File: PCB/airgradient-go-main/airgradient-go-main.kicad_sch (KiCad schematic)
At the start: 198 parts, among them CN3 SM05B-SRSS-TB (LF)(SN), CN4 SM05B-SRSS-TB (LF)(SN), CN5 SM05B-SRSS-TB (LF)(SN), Q1 SIA445EDJ-T1-GE3, Q2 ZVN4106FTA_C508255, Q3 CSD83325L, Q4 SS8050-G, Q5 SI1308EDL, SW1 TS-1091C-A1B3-D2, SW2 TS-1091C-A1B3-D2, U1 W25N512GVEIG, U10 SGP41-D-R4, U11 PS1-CO-SMOKE-10k, U12 SHT4x, U13 SPL07-003, U14 LIS2DH12TR, U15 TMUX121NKGR_C22428404, U16 S12, U17 TCA6408ARGT, U18 TAU1113, U19 LM66200DRLR, U2 ZDSD512MLGEAG, U20 LP5036, U3 BQ27742YZFR-G1, U4 ESP32-C5-MINI-1, U5 BQ25628RYKR, U6 HYG-8503A, U7 TPL5010DDCR, U8 TPS63802DLAR, U9 TPS7A0228DQNR

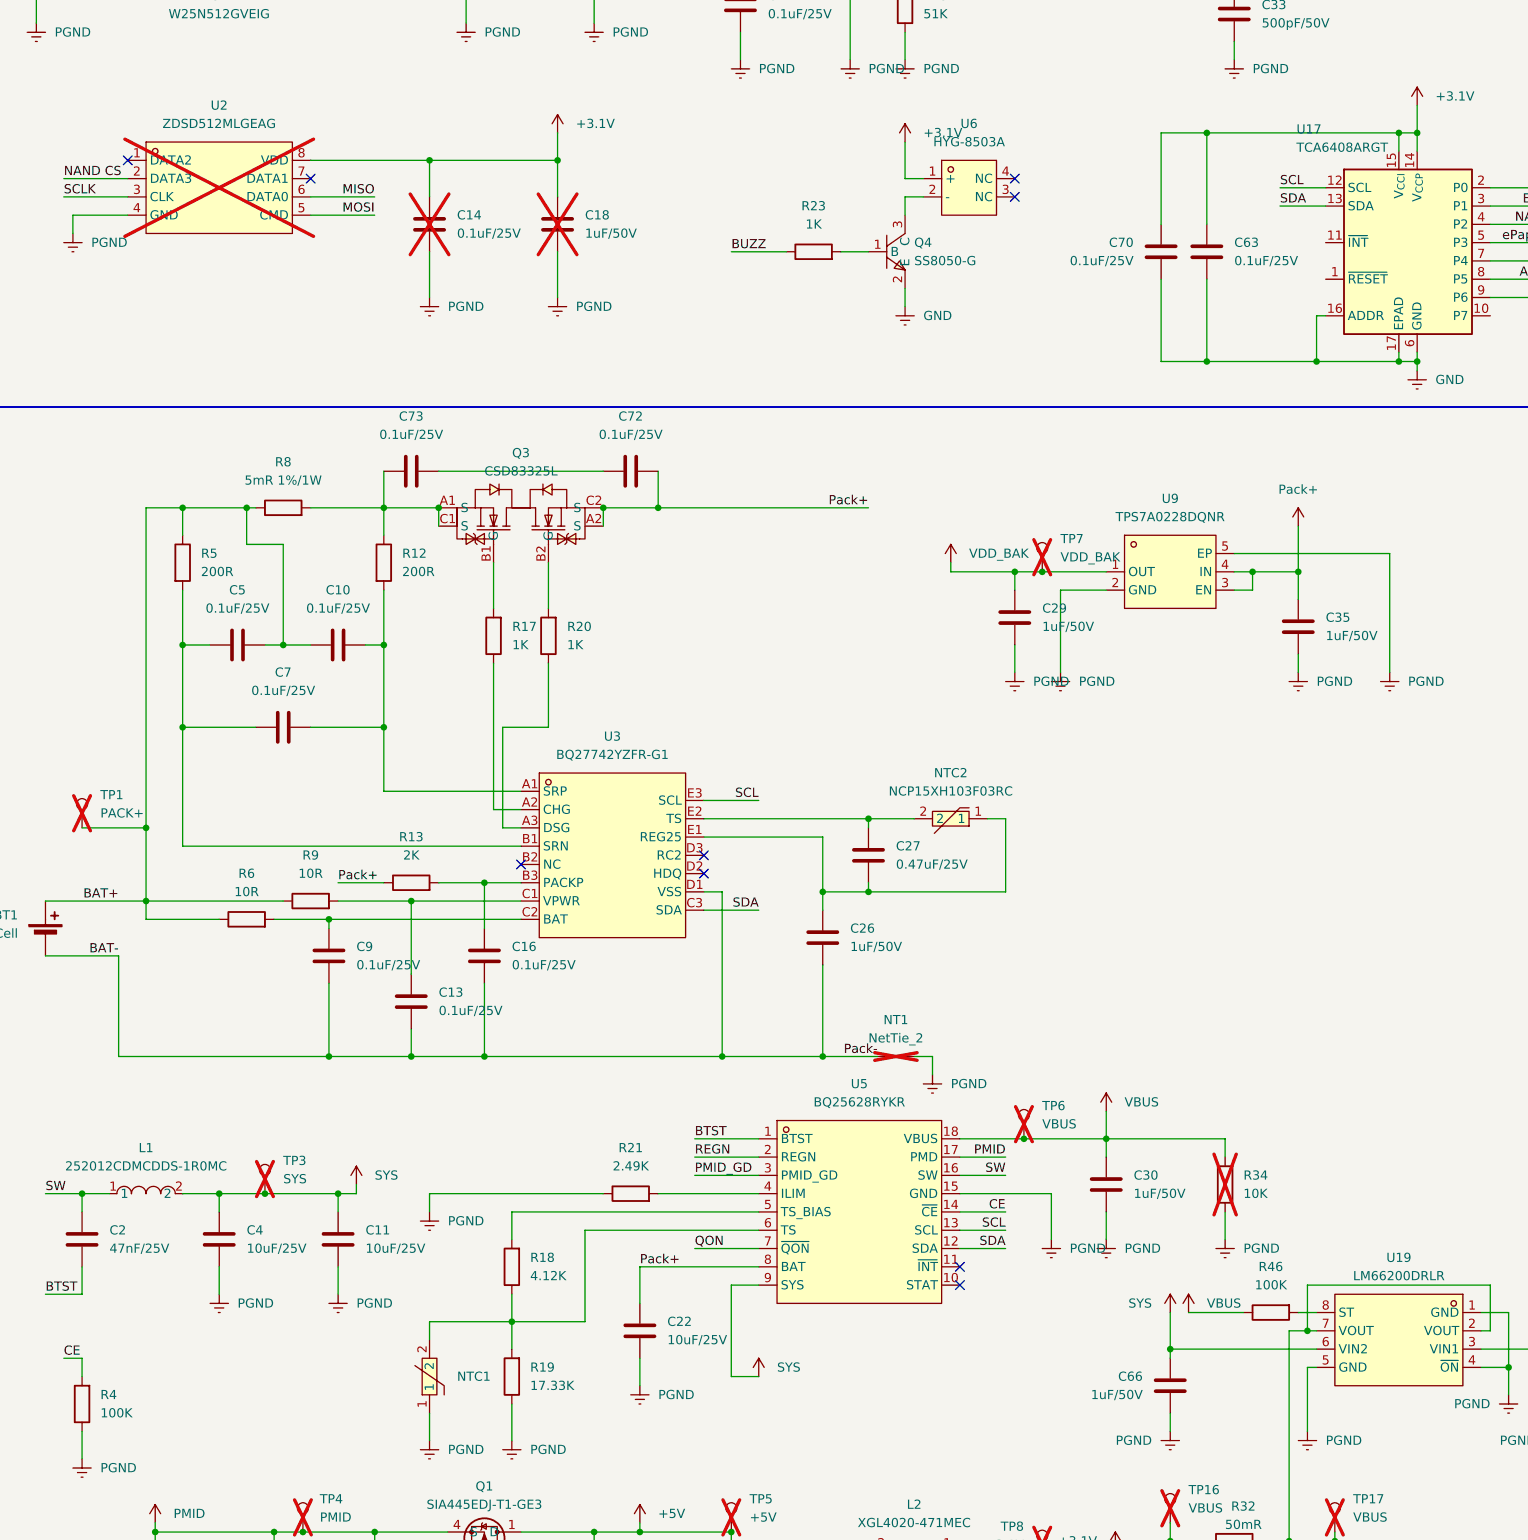
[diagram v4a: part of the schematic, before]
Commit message: v2.1: post-prototype fixes from v2.0 review and issue #1
- Battery: add C75 (100nF 0402) from BAT+ to GND at the battery +
  terminal as an RF shunt, with a GND via next to it
- NTC1 moved next to the battery negative tab (B.Cu), part changed
  to NCP15XH103F03RC; BQ25628 TS divider R18/R19 = 5.23k/30.1k
- Add R60 100K pull-up on TCA6408 RESET
- BOM: fix LCSC part numbers that were shared across different values
  (R13 2K -> C4109, R5/R12 200R -> C25087, 100K group -> C60491,
  C17/C21/C27 corrected)
- Remove test point footprints that were placed outside the board
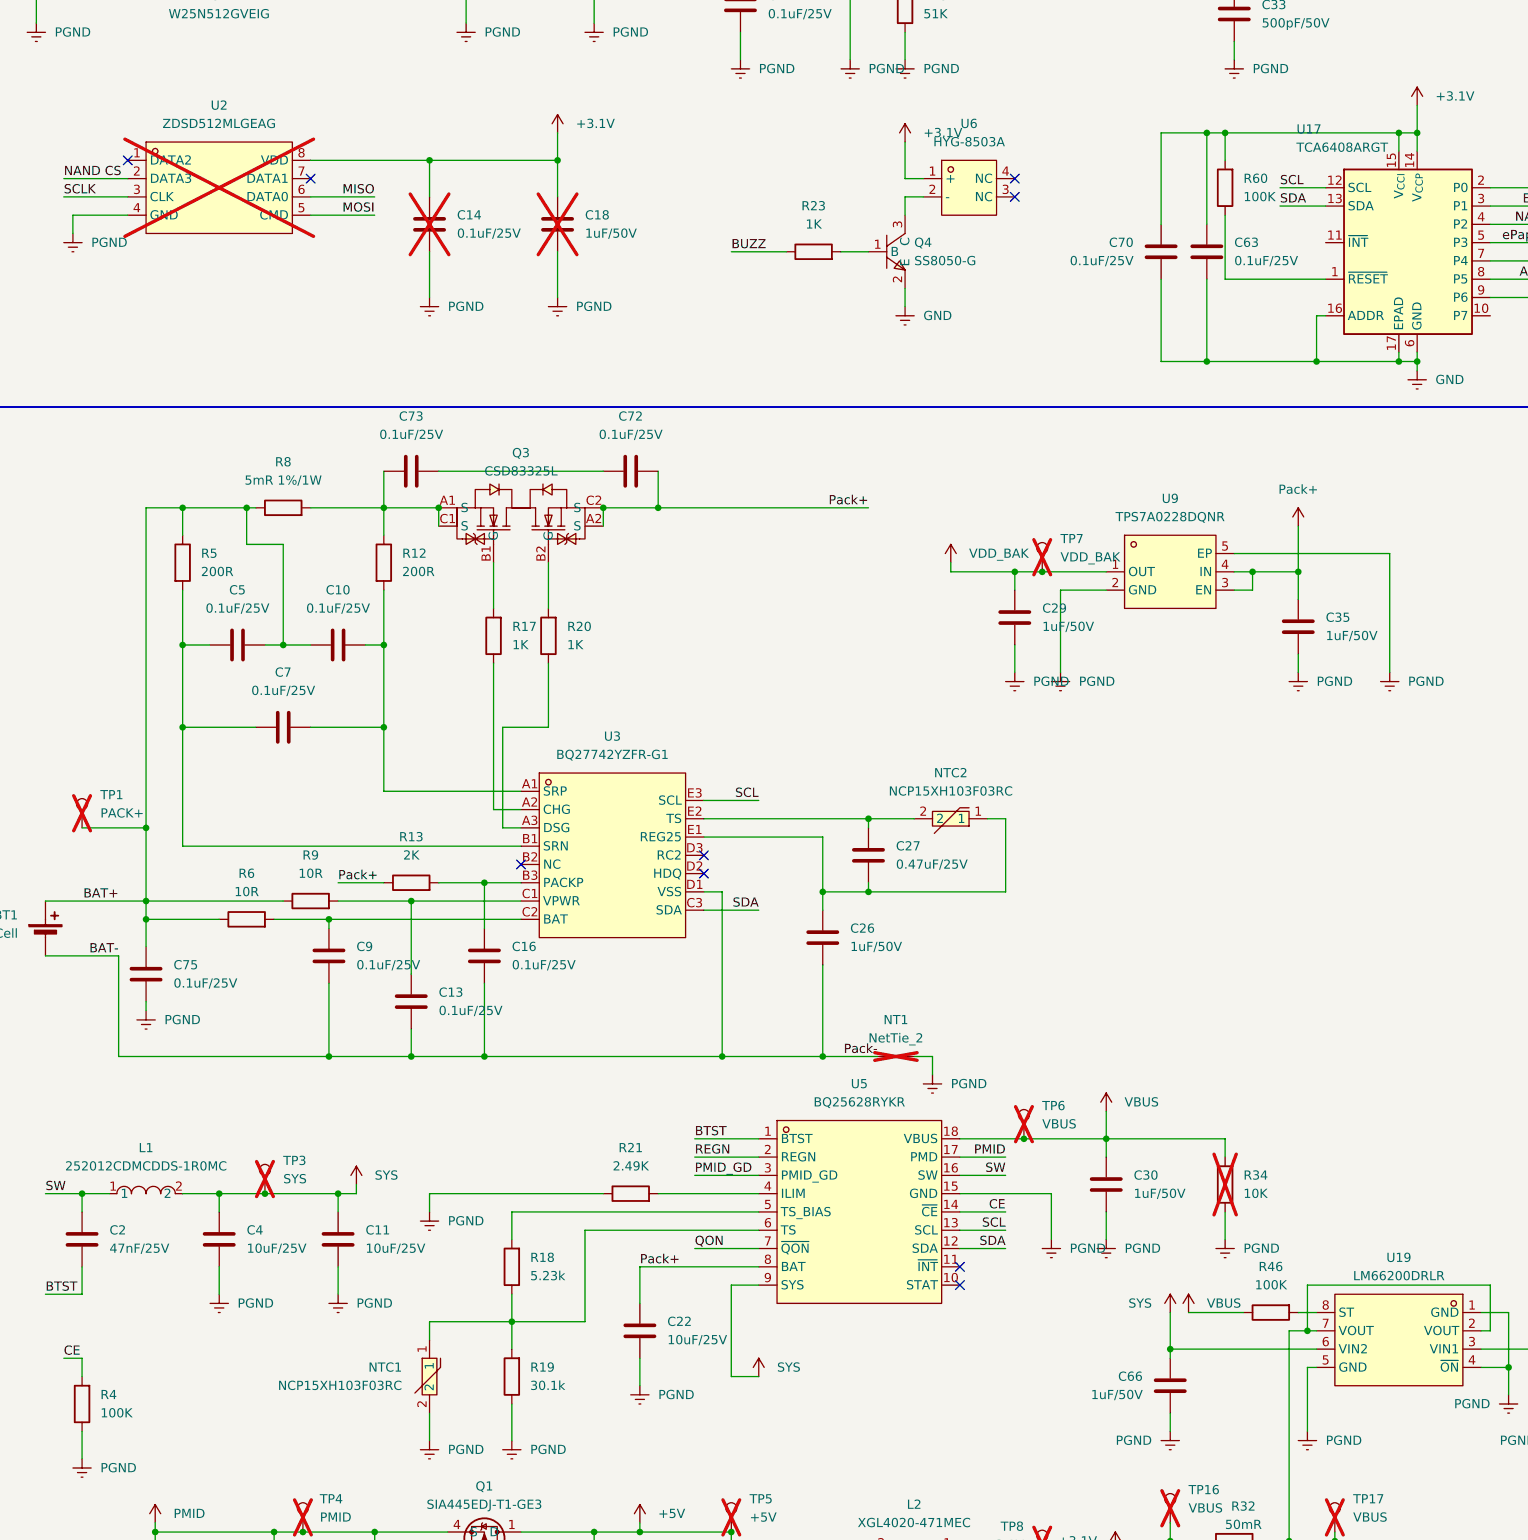
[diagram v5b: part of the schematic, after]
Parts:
- removed NTC1: KNTC0805/10KF3950, easyeda2kicad-oaf:R0805, symbol easyeda2kicad-oaf:KNTC0805_10KF3950
- added C75: 0.1uF/25V, Capacitor_SMD:C_0402_1005Metric, symbol Device:C
- added NTC1: NCP15XH103F03RC, easyeda2kicad-oaf:R0402, symbol easyeda2kicad-oaf:NCP15XH103F03RC
- added R60: 100K, Resistor_SMD:R_0402_1005Metric, symbol Device:R
- AE1, U10, U12, U16: now in the parts list
- C17: LCSC Part C315248 -> C100072
- C21: LCSC Part C315248 -> C6119813
- C27: LCSC Part C7500380 -> C2934765
- R12, R5: LCSC Part (none) -> C25087
- R13: LCSC Part C106235 -> C4109
- R14, R2, R3, R33, R38, R44, R59: LCSC Part C327797 -> C60491
- R18: value 4.12K -> 5.23k
- R19: value 17.33K -> 30.1k
- R32: LCSC Part C106231 -> C247602
- R35: LCSC Part C106231 -> C705493
- R6, R9: LCSC Part C106235 -> C25077
- R8: LCSC Part (none) -> C2988648
- U17: LCSC Part (none) -> C181499
- U20: LCSC Part (none) -> C701961
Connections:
- net +3.1V: now also R60.2
- net BAT+: now also C75.1
- net GND: now also C75.2, NTC1.2
- net at R18.1, R19.2, U5.6 (TS): now also NTC1.1
- net at U17.1 (~{RESET}): now also R60.1

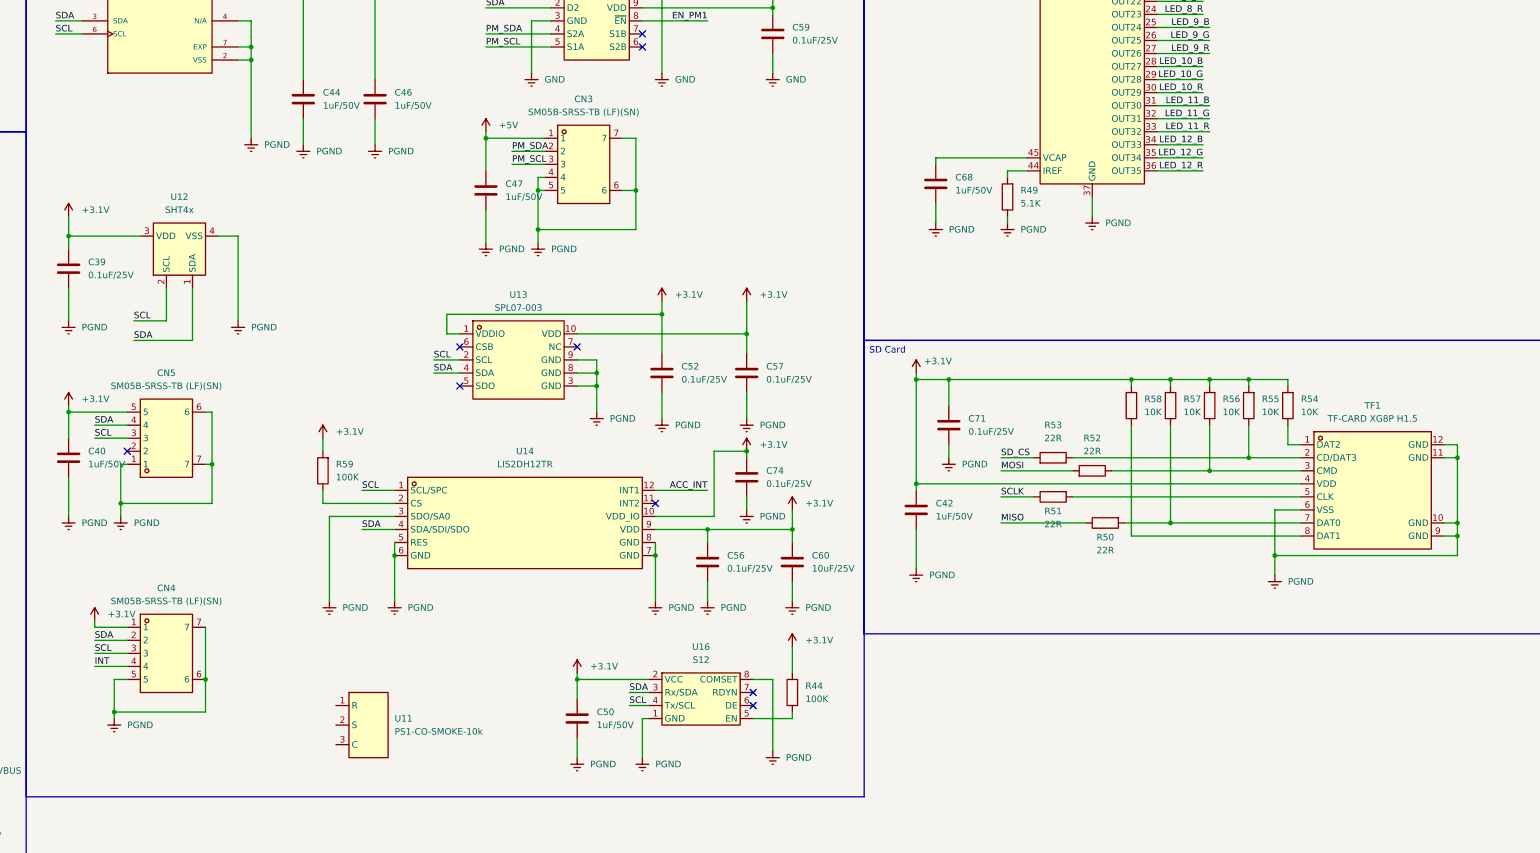
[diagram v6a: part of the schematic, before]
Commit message: v2.1: switch 5-pin connectors to HCZZ0032-5, DNP SD card
- CN1/CN2/CN3 are now HCZZ0032-5 (replaces SM05B-SRSS-TB CN3/CN4/CN5)
- SD card not populated: TF1, R50-R58, C42, C71 set to DNP
- BOM.csv regenerated

Known issues (to fix before production):
- CN2 pad 7 (GND) overlaps the /SCL trace on F.Cu (DRC short)
- 6 footprint attribute mismatches vs schematic (exclude-from-BOM /
  DNP on AE1, BT1, U10, U11, U12, U18) - run Update PCB from Schematic
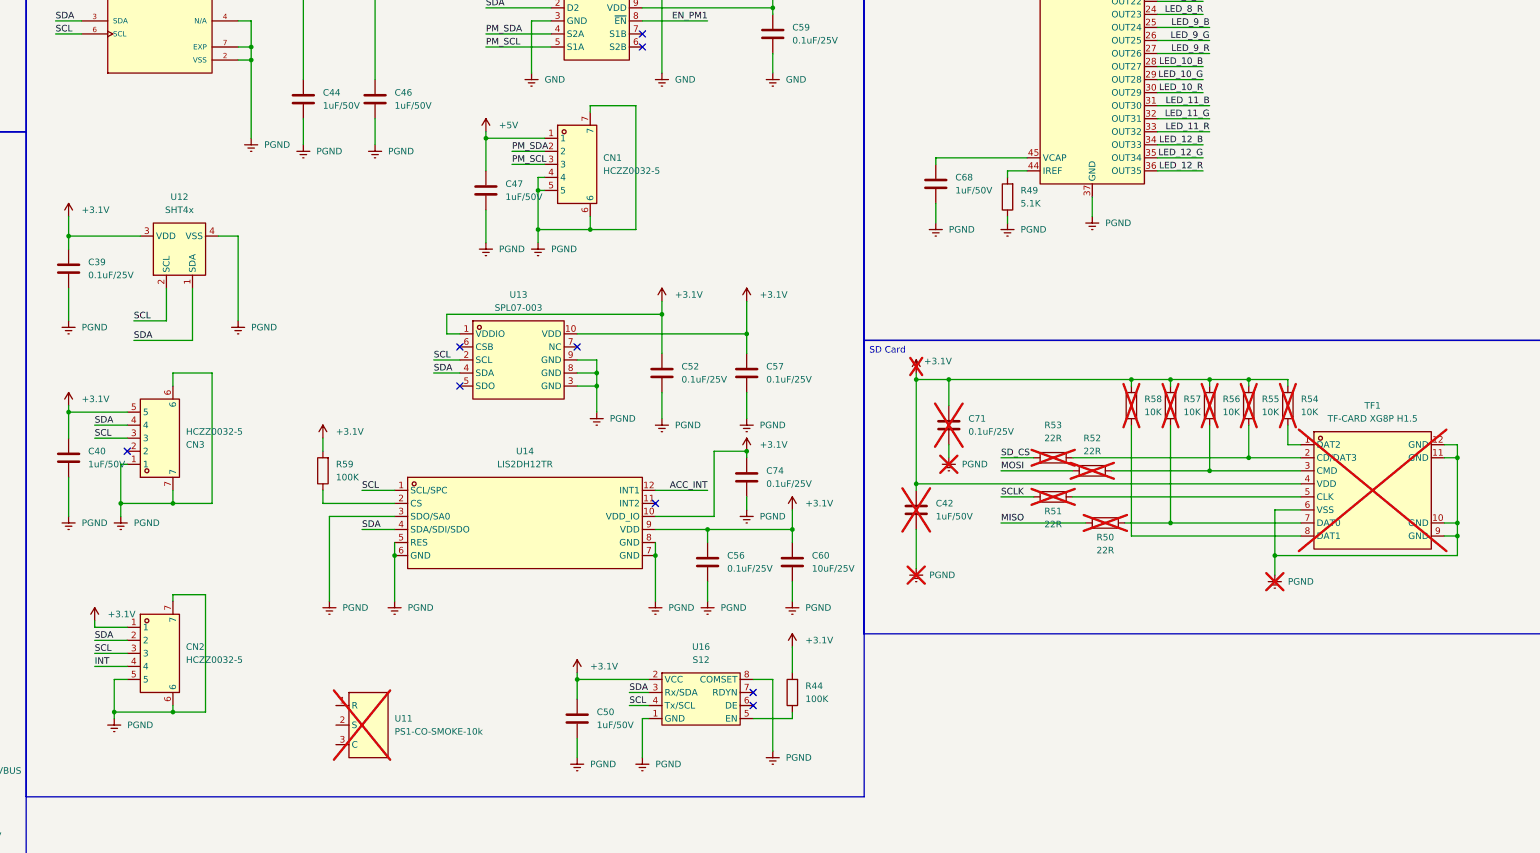
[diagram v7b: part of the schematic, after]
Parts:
- removed CN3, CN4, CN5: SM05B-SRSS-TB (LF)(SN), easyeda2kicad-oaf:CONN-SMD_SM05B-SRSS-TB-LF-SN, symbol easyeda2kicad-oaf:SM05B-SRSS-TB(LF)(SN)
- added CN1, CN2, CN3: HCZZ0032-5, easyeda2kicad-oaf:CONN-SMD_HCZZ0032-5, symbol easyeda2kicad-oaf:HCZZ0032-5
- AE1, BT1, U10, U12, U18: now left out of the parts list
- C42, C71, R50, R51, R52, R53, R54, R55, R56, R57, R58, TF1, U11: now not fitted
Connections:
- net +3.1V: now also CN2.1, CN3.5
- net +5V: now also CN1.1
- net GND: now also CN1.4, CN1.5, CN1.6, CN1.7, CN2.5, CN2.6, CN2.7, CN3.1, CN3.6, CN3.7
- net INT: now also CN2.4
- net PM_SCL: now also CN1.3
- net PM_SDA: now also CN1.2
- net SCL: now also CN2.3, CN3.3
- net SDA: now also CN2.2, CN3.4

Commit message: wip: checkpoint before Mac migration
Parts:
- U16: footprint S12-oaf:S12 -> S12-oaf:S12_rev2
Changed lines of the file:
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@@
 			)
 		)
-		(property "Footprint" "S12-oaf:S12"
+		(property "Footprint" "S12-oaf:S12_rev2"
 			(at 392.43 314.96 0)
 			(hide yes)
@@
 			)
 		)
-		(property "Description" "New 2026 Senseair CO2 sensor"
+		(property "Description" "Senseair S12 CO2 sensor (art. 012-0-0001). Pin 6 = EEPA (EEPROM access output) from rev 2.00 per PCN16844, DE on rev 1.00. Footprint S12 = rev 1.00 land pattern, S12_rev2 = rev 2.00 land pattern."
 			(at 389.89 312.42 0)
 			(hide yes)
